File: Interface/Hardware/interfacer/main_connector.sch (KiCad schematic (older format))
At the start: 6 parts, among them J19 left top conn, J20 right top conn, J8 left bottom conn, J9 right bottom conn

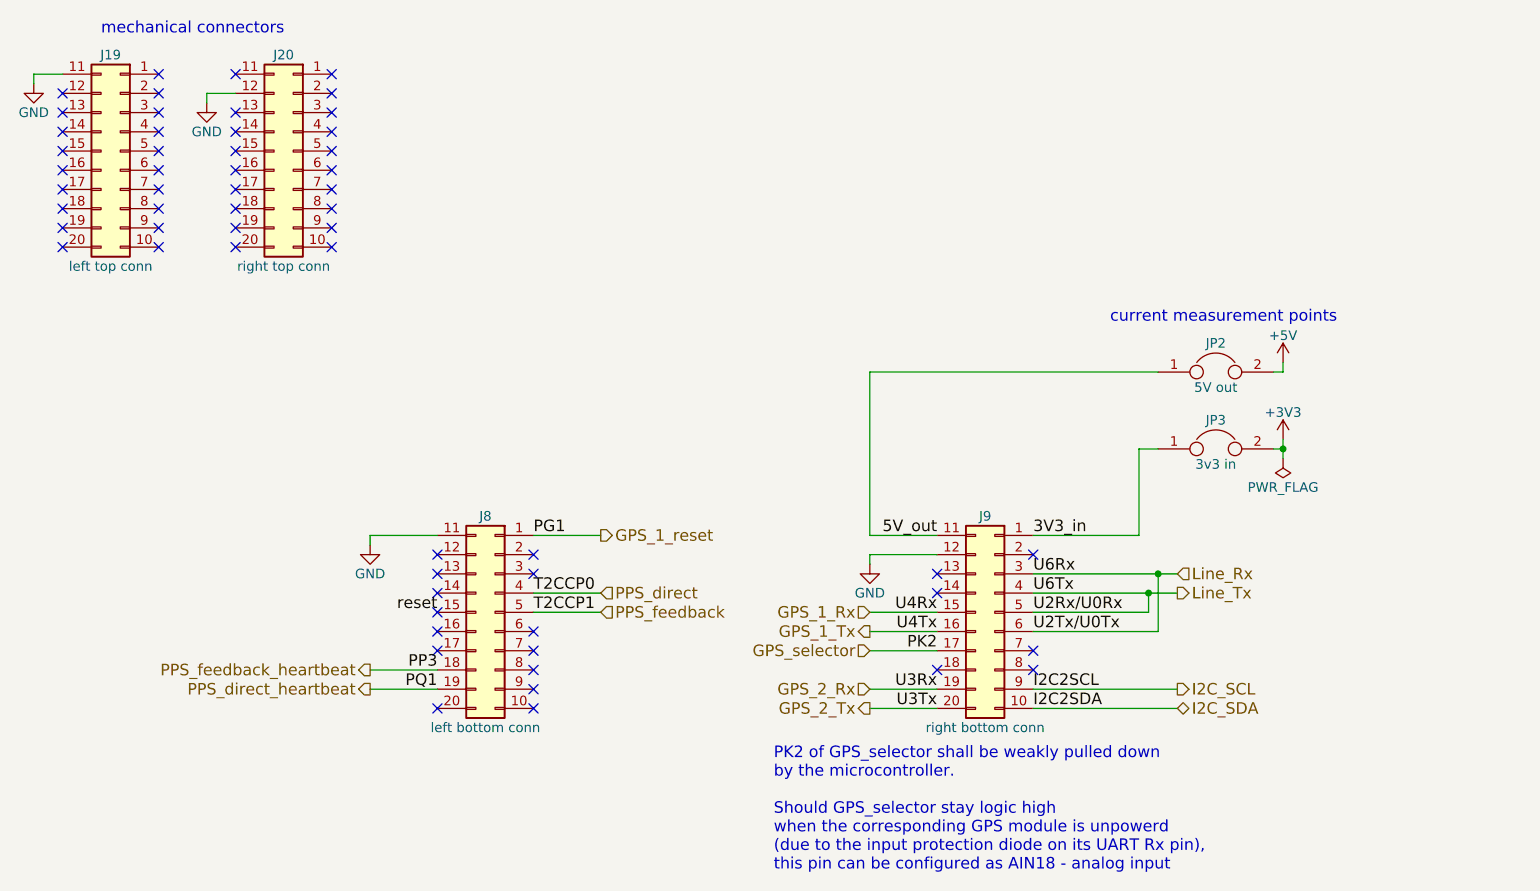
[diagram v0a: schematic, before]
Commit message: added pin names to the main connector
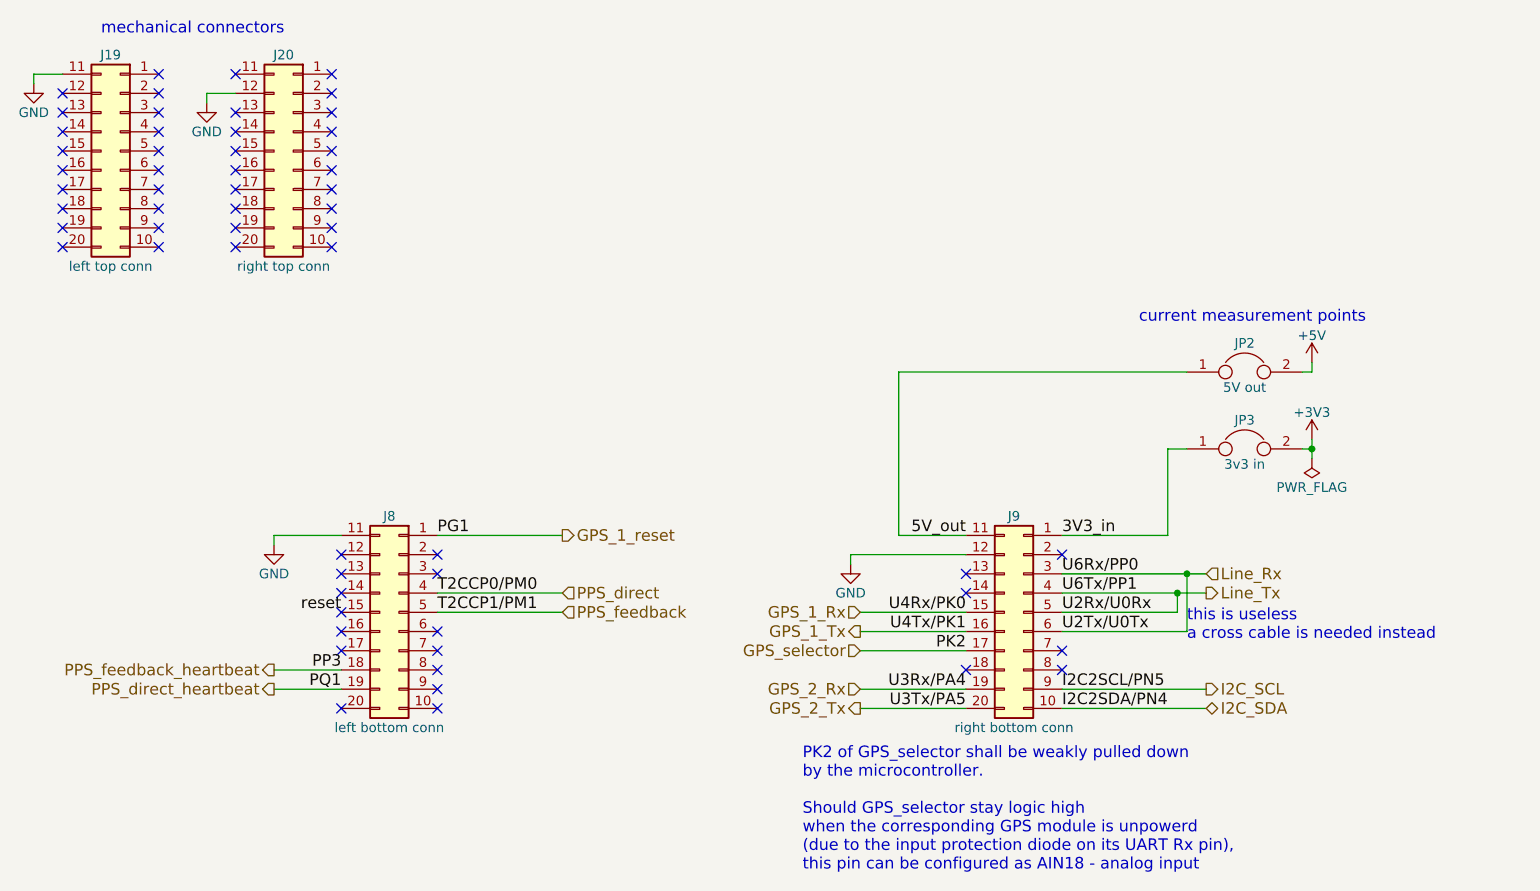
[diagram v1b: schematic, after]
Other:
- note added: "this is useless\na cross cable is needed instead"
- moved on the sheet: J8, J9, JP2, JP3

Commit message: line UART out
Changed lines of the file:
@@
 	4000 4050 4650 4050
 Wire Wire Line
-	7250 3850 7900 3850
+	7250 3850 8000 3850
 Wire Wire Line
-	7900 3850 8000 3850
-Wire Wire Line
-	7250 3950 7850 3950
-Wire Wire Line
-	7850 3950 8000 3950
+	7250 3950 8000 3950
 Wire Wire Line
 	7250 4450 8000 4450
@@
 Connection ~ 8550 3200
 Wire Wire Line
-	8550 3150 8550 3200
-Wire Wire Line
-	8550 3200 8550 3250
+	8550 3150 8550 3250
 Wire Wire Line
 	2050 1250 1900 1250
